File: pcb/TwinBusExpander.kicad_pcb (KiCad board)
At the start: 4 copper layers, 38.8 x 22.5 mm, 30 parts, among them J1 USB_C_Receptacle_USB2.0_16P, J2 Twinbus 7630, Q1 AO3400A, SW1 Reset, SW2 Boot, U1 PC817X3C, U2 PC817X3C, U3 AMS1117-3.3, U4 ESP32-C6-WROOM-1

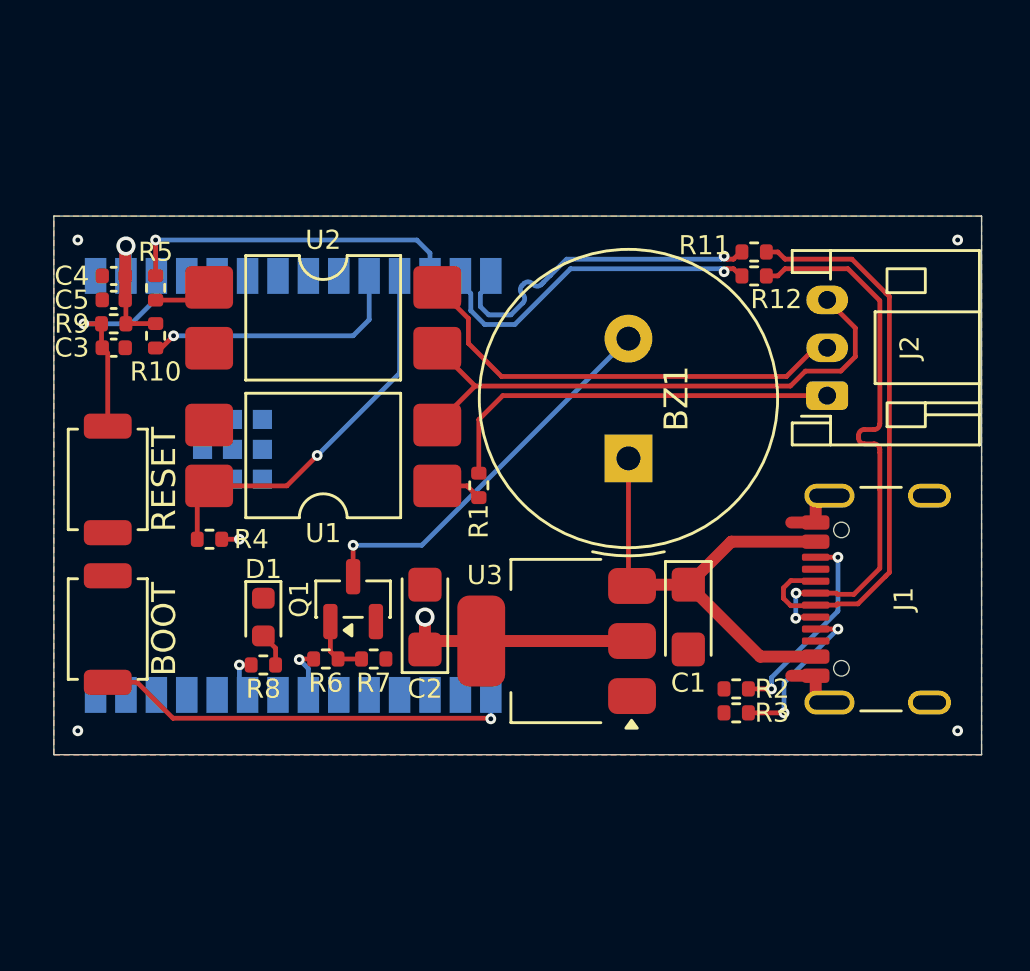
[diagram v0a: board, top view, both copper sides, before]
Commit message: feat!: remove speaker completely
Speaker didnt work as planned, removed. Board got a lot smaller.
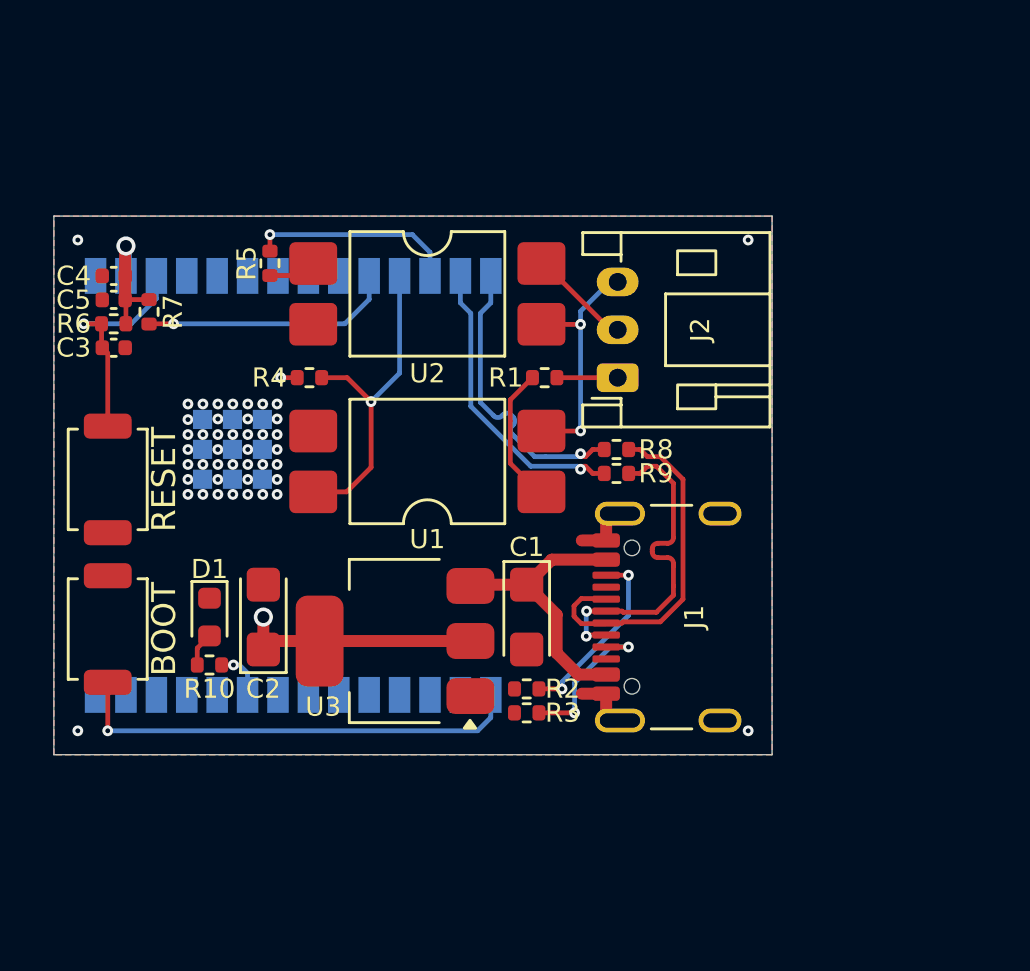
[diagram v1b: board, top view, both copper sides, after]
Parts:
- removed BZ1: Buzzer, Buzzer_Beeper:Buzzer_TDK_PS1240P02BT_D12.2mm_H6.5mm
- removed Q1: AO3400A, Package_TO_SOT_SMD:SOT-23
- removed the R6 at (101.4, 82.2)
- removed the R7 at (103.4, 82.2)
- removed REF**: OSHW-Logo_5.7x6mm_SilkScreen, Symbol:OSHW-Logo_5.7x6mm_SilkScreen
- moved R8 10.1 mm to (113.5, 73.5)
- moved R9 10.1 mm to (113.5, 74.5)
- moved J1 8.78 mm to (116.8, 80.5)
- moved J2 8.78 mm to (113.5, 70.5)
- moved R2 8.75 mm to (109.8, 83.5)
- moved R3 8.75 mm to (109.8, 84.5)
- moved R4 7.94 mm to (100.7, 70.5), turned to 180 degrees
- moved C1 6.75 mm to (109.8, 80.5)
- moved C2 6.75 mm to (98.8, 80.5)
- moved U3 6.75 mm to (104.2, 81.5)
- moved R1 5.27 mm to (110.5, 70.5), turned to 180 degrees
- moved R5 4.88 mm to (99.0, 65.7)
- moved U2 4.46 mm to (105.6, 67.0)
- moved U1 4.36 mm to (105.6, 74.0)
- moved G*** 2.47 mm to (115.8, 80.5), turned to -90 degrees
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- renumbered R8 to R10, R9 to R6, R10 to R7, R11 to R8, R12 to R9
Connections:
- U4 pad 21: /Buzzer -> unconnected-(U4-GPIO23-Pad21)
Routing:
- net Net-(BZ1--): track 16.4 -> 0.00 mm, vias 1 -> 0
- net /TB_Bell: track 17.2 -> 2.54 mm
- net /TB_Door: track 18.9 -> 4.33 mm
- net /TB_GND: track 23.8 -> 10.3 mm, vias 0 -> 2
- net /USB_D-: track 23.8 -> 14.1 mm
- net /USB_D+: track 24.5 -> 14.8 mm
- net VBUS: track 20.4 -> 11.9 mm
- net /Door: track 14.1 -> 8.67 mm
- net /TB_B: track 1.94 -> 5.76 mm
- net /~{Bell}: track 16.6 -> 13.8 mm
- net /BzGt: track 2.68 -> 0.00 mm
- net /Buzzer: track 2.24 -> 0.00 mm, vias 1 -> 0
- net /ESP_D+: track 14.3 -> 12.4 mm
- net /ESP_D-: track 14.4 -> 12.5 mm
- net /Boot: track 17.6 -> 19.2 mm
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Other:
- board size 38.8 x 22.5 mm -> 30 x 22.5 mm

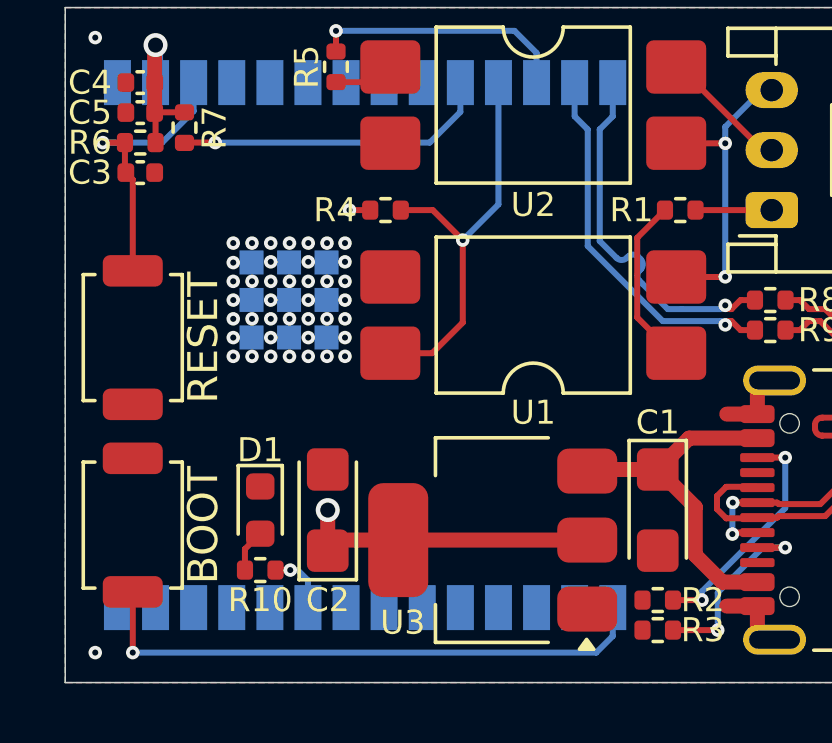
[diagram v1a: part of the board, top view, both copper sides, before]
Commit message: feat: replace Optoisolators
Replace generic PC817 with LTV-817S because of part availability
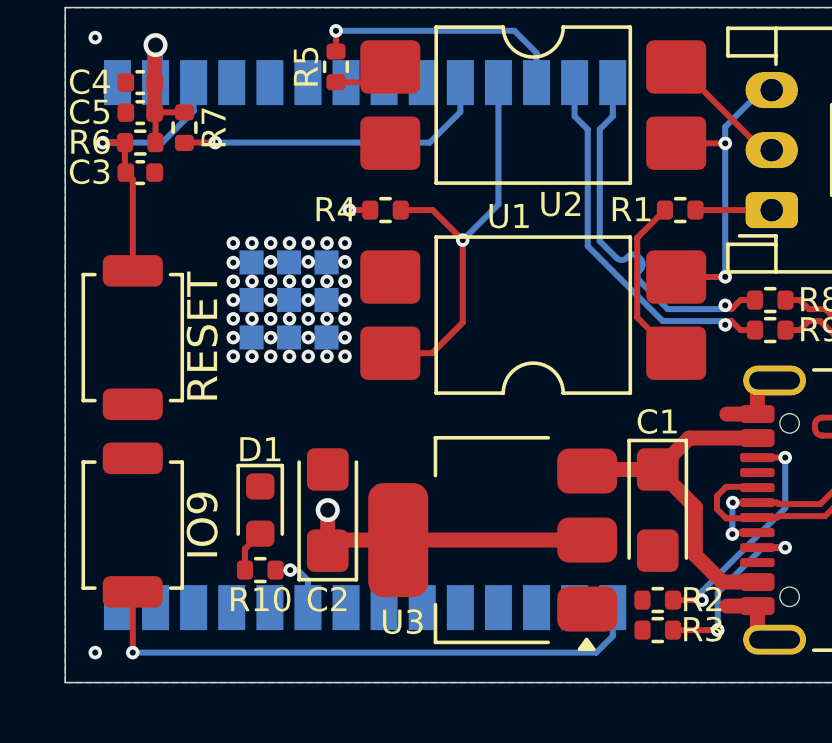
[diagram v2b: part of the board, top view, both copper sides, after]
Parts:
- U1, U2: value PC817X3C -> LTV-817S
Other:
- board text added: "IO9"
- board text removed: "BOOT"

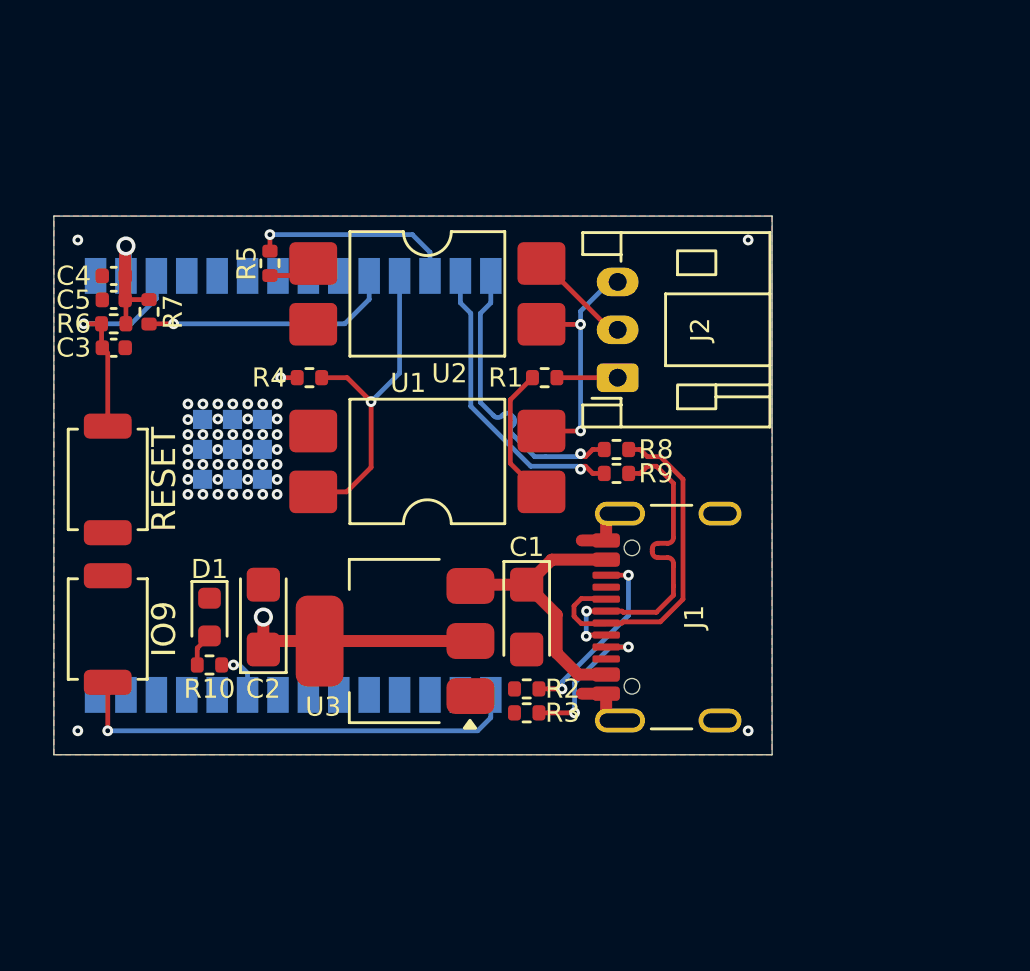
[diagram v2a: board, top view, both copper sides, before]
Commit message: feat: add edge rails
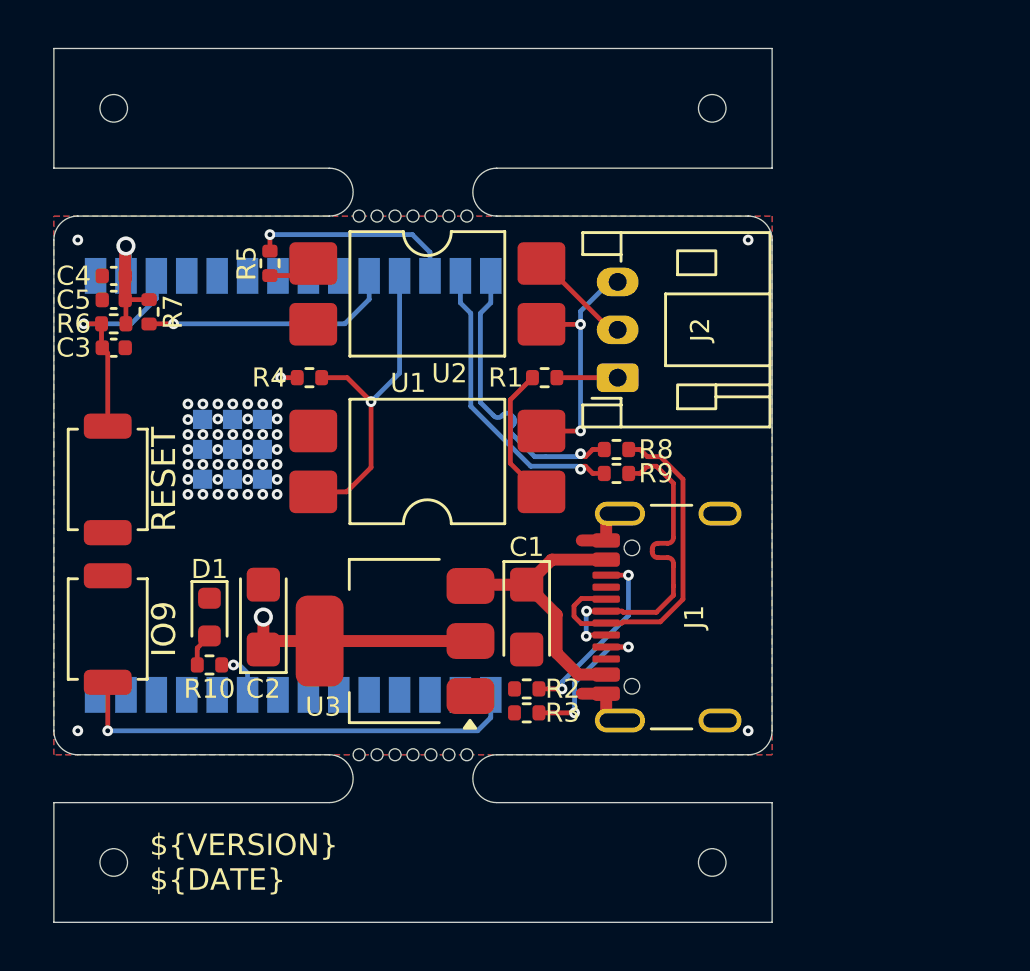
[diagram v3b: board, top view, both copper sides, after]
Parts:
- added REF**: JLCPCB_Tooling_Hole, My_Footprints:JLCPCB_Tooling_Hole, F.Cu at (92.5, 59.2)
- added REF**: JLCPCB_Tooling_Hole, My_Footprints:JLCPCB_Tooling_Hole, F.Cu at (92.5, 90.8)
- added REF**: JLCPCB_Tooling_Hole, My_Footprints:JLCPCB_Tooling_Hole, F.Cu at (117.5, 59.2)
- added REF**: JLCPCB_Tooling_Hole, My_Footprints:JLCPCB_Tooling_Hole, F.Cu at (117.5, 90.8)
- added mouse-bite-2mm-slot: VAL**, Panelization:mouse-bite-2x5mm-slot-onesided-v2, F.Cu at (105.0, 87.2)
- added mouse-bite-2mm-slot: VAL**, Panelization:mouse-bite-2x5mm-slot-onesided-v2, F.Cu at (105.0, 62.8)
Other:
- board size 30 x 22.5 mm -> 30 x 36.5 mm
